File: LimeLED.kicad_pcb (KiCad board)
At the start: 2 copper layers, 91.2 x 79 mm, 16 parts, among them CN1 HB9500-3, CN2 HB9500-3, U1 ESP32-DEVKITC-32D, U2 TPSM863257RDXR, U3 220k, U4 SN74AHCT125N

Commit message: add input protection and plotted schematic
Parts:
- added C7: 25V470UF, Capacitor_THT:CP_Radial_D8.0mm_P3.50mm, F.Cu at (78.3, 102.0)
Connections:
- CN2 pad 1: +12V -> Net-(CN2-Pad1)
- CN2 pad 2: +12V -> Net-(CN2-Pad1)
- CN2 pad 3: +12V -> Net-(CN2-Pad1)
- F1 pad 1: unconnected-(F1-Pad1) -> Net-(CN2-Pad1)
- F1 pad 2: unconnected-(F1-Pad2) -> +12V

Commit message: wire connections
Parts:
- added C8: 100nF 25v, Capacitor_SMD:C_0402_1005Metric, F.Cu at (81.5, 82.5)
- added D1: SSA34, Diode_SMD:D_SMA, F.Cu at (81.0, 75.8)
- added F2: 500mA, easyeda2kicad:F1206, F.Cu at (78.8, 82.0)
- C7: value 25V470UF -> 470uF 25v
- F1: value Fuse -> 30A Medium Fuse Holder
- moved C7 58.4 mm to (134.2, 118.8)
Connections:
- C1 pad 2: +12V -> Net-(D1-K)
- C2 pad 1: +12V -> Net-(D1-K)
- R1 pad 1: +12V -> Net-(D1-K)
- U2 pad 1: +12V -> Net-(D1-K)
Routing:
- net GND: track 0.00 -> 281.2 mm
- net +5V: track 0.00 -> 87.0 mm
- net +12V: track 0.00 -> 74.8 mm
- net Net-(CN2-Pad1): track 0.00 -> 45.9 mm
- net Net-(D1-K): track 0.00 -> 31.6 mm
- net Net-(U2-EN): track 0.00 -> 9.13 mm
- net Net-(C3-Pad1): track 0.00 -> 8.66 mm
- net Net-(U2-FB): track 0.00 -> 7.00 mm

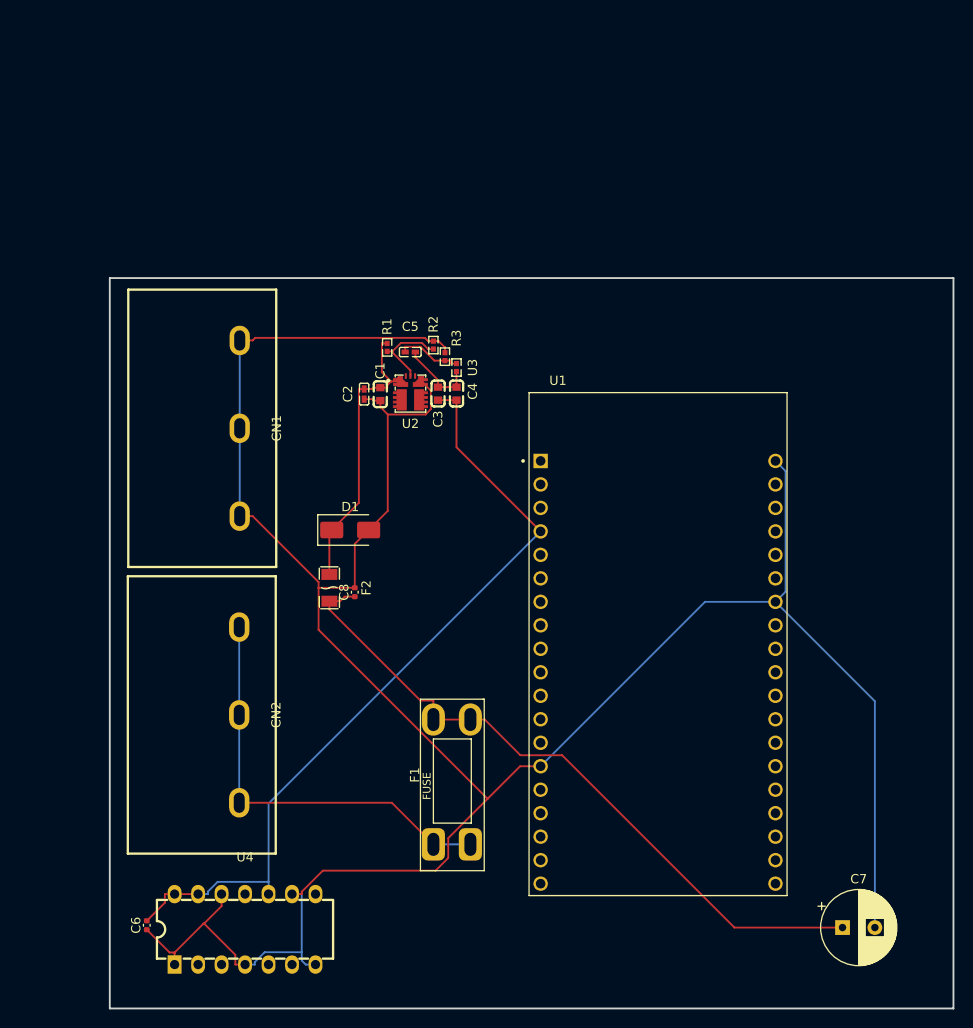
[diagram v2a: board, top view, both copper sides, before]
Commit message: add relay
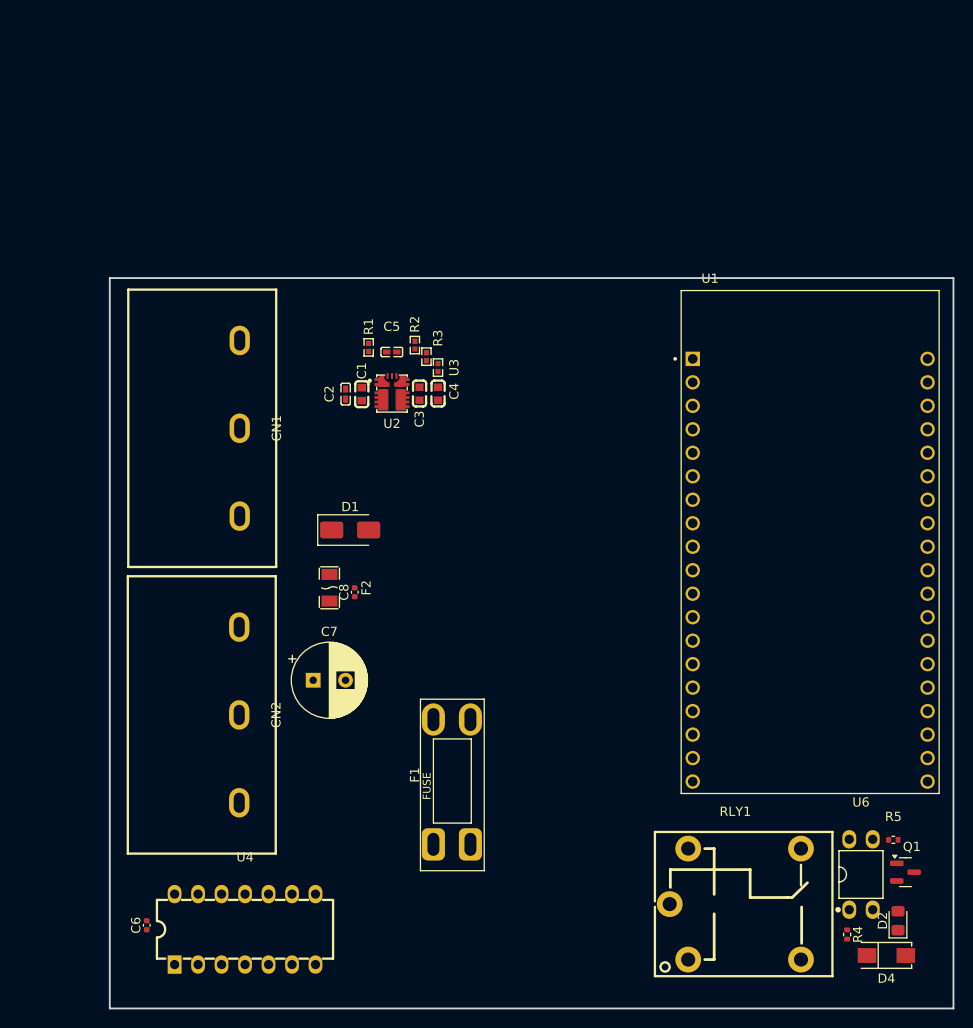
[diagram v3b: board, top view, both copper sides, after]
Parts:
- added D2: RED_LED, LED_SMD:LED_0805_2012Metric_Pad1.15x1.40mm_HandSolder, F.Cu at (140.2, 118.0)
- added D4: 1N4007, easyeda2kicad:SMA_L4.3-W2.5-LS5.0-RD, F.Cu at (139.0, 121.8)
- added Q1: SS8050, Package_TO_SOT_SMD:SOT-23, F.Cu at (141.1, 112.8)
- added R4: 1K, Resistor_SMD:R_0402_1005Metric, F.Cu at (134.8, 119.5)
- added R5: 1K, Resistor_SMD:R_0402_1005Metric, F.Cu at (139.8, 109.3)
- added RLY1: SRD-05VDC-SL-C, easyeda2kicad:RELAY-TH_SRD-XXVDC-XL-C, F.Cu at (122.7, 116.2)
- added U6: PC817C_C3025068, easyeda2kicad:DIP-4_L4.6-W6.5-P2.54-LS7.6-BL, F.Cu at (136.2, 113.0)
- moved C7 63.2 mm to (77.0, 92.0)
- moved U1 19.8 mm to (130.8, 77.0)
- moved C1 2.00 mm to (82.3, 61.0)
- moved C2 2.00 mm to (80.5, 61.0)
- moved C3 2.00 mm to (88.5, 61.0)
- moved C4 2.00 mm to (90.5, 61.0)
- moved C5 2.00 mm to (85.5, 56.5)
- moved R1 2.00 mm to (83.0, 56.0)
- moved R2 2.00 mm to (88.0, 55.8)
- moved R3 2.00 mm to (89.2, 57.0)
- moved U2 2.00 mm to (85.5, 60.4)
- moved U3 2.00 mm to (90.5, 58.2)
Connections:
- U1 pad J2-5: unconnected-(U1-IO34-PadJ2-5) -> GPIO_34
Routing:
- net GND: track 281.2 -> 0.00 mm
- net +5V: track 87.0 -> 0.00 mm
- net +12V: track 74.8 -> 0.00 mm
- net Net-(CN2-Pad1): track 45.9 -> 0.00 mm
- net Net-(D1-K): track 31.6 -> 0.00 mm
- net Net-(U2-EN): track 9.13 -> 0.00 mm
- net Net-(C3-Pad1): track 8.66 -> 0.00 mm
- net Net-(U2-FB): track 7.00 -> 0.00 mm

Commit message: add 64p PSU connector
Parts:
- added CN3: ER64BGFBK, easyeda2kicad:CONN-TH_64P-P2.54_ER64BGFBK, F.Cu at (98.9, 38.3)
- added D3: LED Red, LED_THT:LED_D3.0mm_Horizontal_O6.35mm_Z10.0mm, F.Cu at (87.5, 108.2)
- added D5: LED Green, LED_THT:LED_D3.0mm_Horizontal_O6.35mm_Z10.0mm, F.Cu at (81.5, 108.2)
- added R6: 1K, Resistor_SMD:R_0402_1005Metric, F.Cu at (46.4, 46.5)
- added R7: 220, Resistor_SMD:R_1206_3216Metric, F.Cu at (47.7, 41.4)
- added R9: 21k, Resistor_SMD:R_0603_1608Metric, F.Cu at (46.9, 44.2)
- moved C7 20.0 mm to (97.0, 93.0)
- moved U1 6.72 mm to (126.0, 72.2)
- moved D2 5.84 mm to (136.0, 114.0)
- moved D4 5.84 mm to (134.8, 117.8)
- moved Q1 5.84 mm to (136.8, 108.8)
- moved R4 5.84 mm to (130.5, 115.5)
- moved R5 5.84 mm to (135.5, 105.3)
- moved RLY1 5.84 mm to (118.4, 112.2)
- moved U6 5.84 mm to (132.0, 109.0)
- moved F1 5.80 mm to (90.8, 104.0), turned to 180 degrees
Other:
- board size 91.2 x 79 mm -> 88.2 x 106.8 mm

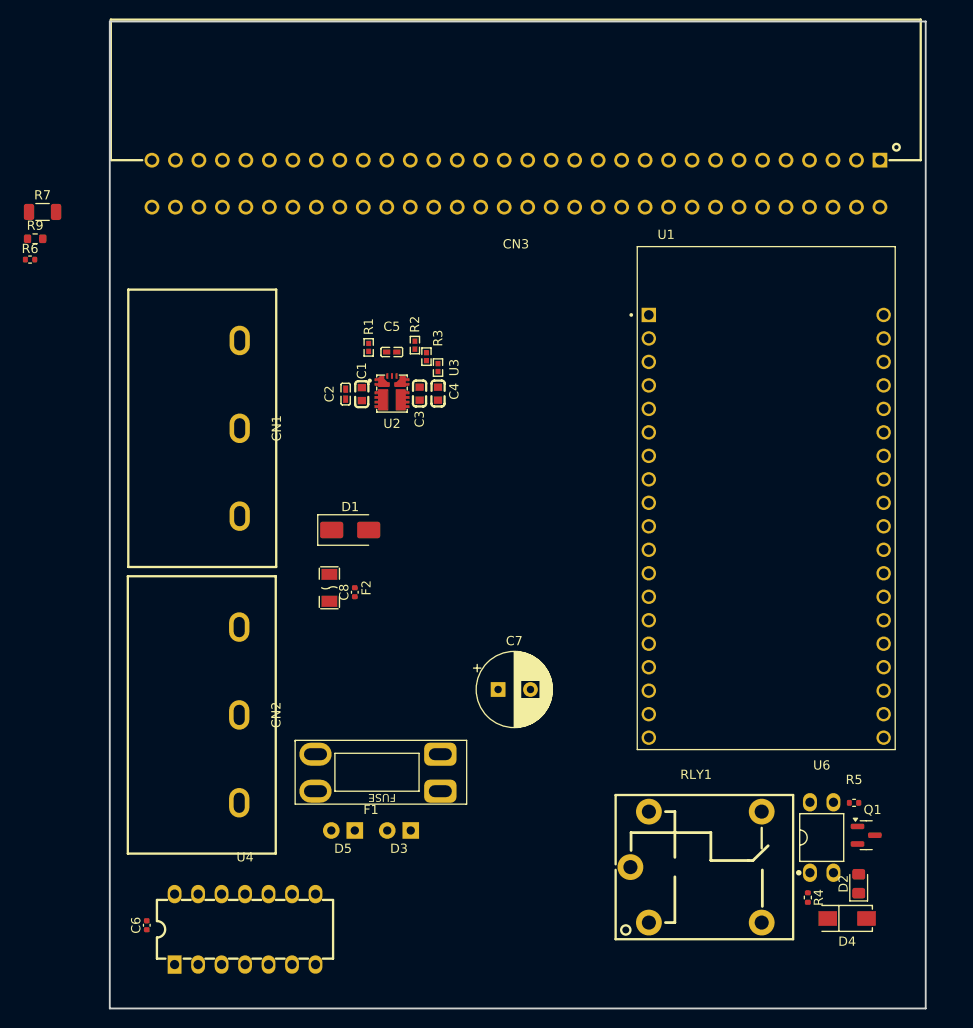
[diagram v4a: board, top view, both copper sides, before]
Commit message: finish input power connector
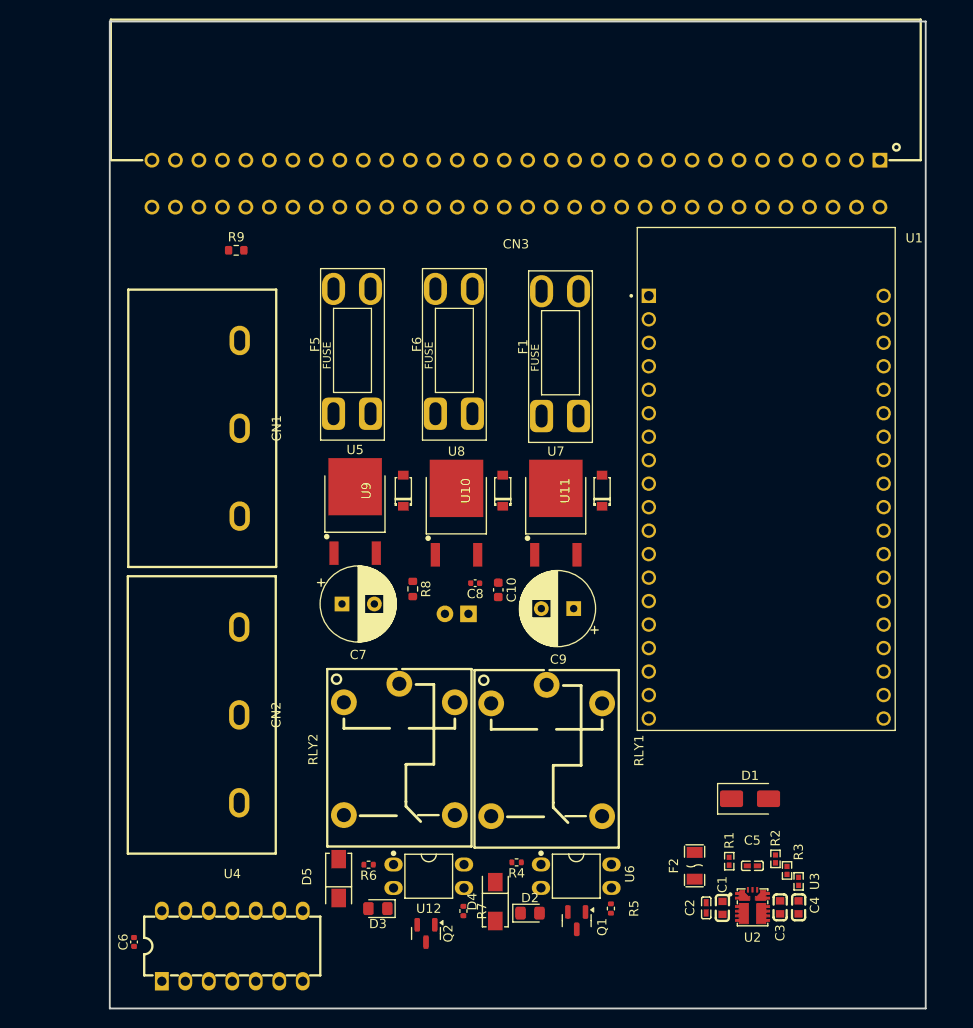
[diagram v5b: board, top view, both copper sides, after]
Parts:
- added C10: 10uF, Capacitor_SMD:C_0603_1608Metric, F.Cu at (97.0, 82.2)
- added C9: 470uF 25v, Capacitor_THT:CP_Radial_D8.0mm_P3.50mm, F.Cu at (105.2, 84.2)
- added D6: LED Red, Custom_footprint:LED_D3.0mm_Horizontal_O6.35mm_Z10.0mm, F.Cu at (93.8, 84.8)
- added F5: 10A Medium Fuse Holder, Custom_footprint:Ebay-Fuse-holder-04mmX15mm-black-auto-fuse-dingus, F.Cu at (79.2, 63.2)
- added F6: 10A, Custom_footprint:Ebay-Fuse-holder-04mmX15mm-black-auto-fuse-dingus, F.Cu at (90.2, 63.2)
- added Q2: SS8050, Package_TO_SOT_SMD:SOT-23, F.Cu at (89.2, 119.4)
- added R8: 2.2k, Resistor_SMD:R_0603_1608Metric, F.Cu at (87.8, 82.1)
- added RLY2: SRD-05VDC-SL-C, easyeda2kicad:RELAY-TH_SRD-XXVDC-XL-C, F.Cu at (86.3, 99.5)
- added U10: SD103AW, easyeda2kicad:SOD-123_L2.8-W1.8-LS3.7-RD, F.Cu at (97.5, 71.5)
- added U11: SD103AW, easyeda2kicad:SOD-123_L2.8-W1.8-LS3.7-RD, F.Cu at (108.2, 71.5)
- added U12: PC817C_C3025068, easyeda2kicad:DIP-4_L4.6-W6.5-P2.54-LS7.6-BL, F.Cu at (89.5, 113.2)
- added U5: MBR20100DT, easyeda2kicad:TO-252-2_L6.5-W6.1-P4.58-LS10.0-BL, F.Cu at (81.5, 74.7)
- added U7: MBR20100DT, easyeda2kicad:TO-252-2_L6.5-W6.1-P4.58-LS10.0-BL, F.Cu at (103.2, 74.8)
- added U8: MBR20100DT, easyeda2kicad:TO-252-2_L6.5-W6.1-P4.58-LS10.0-BL, F.Cu at (92.5, 74.8)
- added U9: SD103AW, easyeda2kicad:SOD-123_L2.8-W1.8-LS3.7-RD, F.Cu at (86.8, 71.5)
- D3: value LED Red -> RED_LED; footprint LED_THT:LED_D3.0mm_Horizontal_O6.35mm_Z10.0mm -> LED_SMD:LED_0805_2012Metric_Pad1.15x1.40mm_HandSolder
- D5: value LED Green -> 1N4007; footprint LED_THT:LED_D3.0mm_Horizontal_O6.35mm_Z10.0mm -> easyeda2kicad:SMA_L4.3-W2.5-LS5.0-RD
- F1: value 30A Medium Fuse Holder -> 10A
- R7: value 220 -> 1K; footprint Resistor_SMD:R_1206_3216Metric -> Resistor_SMD:R_0402_1005Metric
- moved R7 88.3 mm to (93.2, 117.0), turned to 90 degrees
- moved R6 75.0 mm to (83.0, 112.0), turned to 180 degrees
- moved C1 67.9 mm to (121.3, 116.6)
- moved C2 67.9 mm to (119.5, 116.6)
- moved C3 67.9 mm to (127.5, 116.6)
- moved C4 67.9 mm to (129.5, 116.6)
- moved C5 67.9 mm to (124.5, 112.1)
- moved R1 67.9 mm to (122.0, 111.6)
- moved R2 67.9 mm to (127.0, 111.3)
- moved R3 67.9 mm to (128.2, 112.6)
- moved U2 67.9 mm to (124.5, 116.0)
- moved U3 67.9 mm to (129.5, 113.8)
- moved D1 52.1 mm to (124.2, 104.8)
- moved F2 49.6 mm to (118.2, 112.1)
- moved F1 42.0 mm to (101.7, 63.4), turned to 90 degrees
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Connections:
- CN2 pad 1: Net-(D3-A) -> +12V #1
- CN2 pad 2: Net-(D3-A) -> +12V #2
- CN2 pad 3: Net-(D3-A) -> +12V #3
- CN3 pad 1: +12V -> +12V #2
- CN3 pad 10: +12V -> +12V #1
- CN3 pad 11: +12V -> +12V #2
- CN3 pad 12: +12V -> +12V #1
- CN3 pad 13: +12V -> +12V #2
- CN3 pad 14: +12V -> +12V #1
- CN3 pad 15: +12V -> +12V #2
- CN3 pad 16: +12V -> +12V #1
- CN3 pad 17: +12V -> +12V #2
- CN3 pad 18: +12V -> +12V #1
- CN3 pad 19: +12V -> +12V #2
- CN3 pad 2: +12V -> +12V #1
- CN3 pad 20: +12V -> +12V #1
- CN3 pad 21: +12V -> +12V #2
- CN3 pad 22: +12V -> +12V #3
- CN3 pad 23: +12V -> +12V #3
- CN3 pad 24: +12V -> +12V #3
- CN3 pad 25: +12V -> +12V #3
- CN3 pad 26: +12V -> +12V #3
- CN3 pad 27: +12V -> +12V #3
- CN3 pad 28: +12V -> +12V #3
- CN3 pad 29: +12V -> +12V #3
- CN3 pad 3: +12V -> +12V #2
- CN3 pad 30: +12V -> +12V #3
- CN3 pad 31: +12V -> +12V #3
- CN3 pad 32: +12V -> +12V #3
- CN3 pad 4: +12V -> +12V #1
- CN3 pad 5: +12V -> +12V #2
- CN3 pad 54: PSINTERRUPT -> unconnected-(CN3-Pad54)
- CN3 pad 6: +12V -> +12V #1
- CN3 pad 64: PSINTERRUPT -> +12V
- CN3 pad 7: +12V -> +12V #2
- CN3 pad 8: +12V -> +12V #1
- CN3 pad 9: +12V -> +12V #2
- D2 pad 1: GPIO_34 -> RELAY
- D3 pad 1: Net-(D3-K) -> RELAY
- D5 pad 1: Net-(D3-K) -> +5V
- D5 pad 2: +12V -> Net-(D5-A)
- F1 pad 1: Net-(D3-A) -> Net-(U11-A)
- R6 pad 1: GND -> Net-(U12-AN)
- R6 pad 2: Net-(D3-K) -> +5V
- R7 pad 1: Net-(D3-A) -> Net-(Q2-B)
- R7 pad 2: Net-(D3-K) -> Net-(U12-EM)
- U1 pad J2-13: unconnected-(U1-IO12-PadJ2-13) -> RELAY
- U1 pad J2-19: unconnected-(U1-EXT_5V-PadJ2-19) -> +5V
- U1 pad J2-4: +5V -> unconnected-(U1-SENSOR_VN-PadJ2-4)
- U1 pad J2-5: GPIO_34 -> unconnected-(U1-IO34-PadJ2-5)
- U1 pad J3-13: unconnected-(U1-IO4-PadJ3-13) -> LED_DATA_IN_1
- U1 pad J3-15: unconnected-(U1-IO2-PadJ3-15) -> LED_DATA_IN_2
